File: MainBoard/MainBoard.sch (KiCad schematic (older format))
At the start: 57 parts, among them IC1 MAX30102, J3 Conn_01x30_Female, J6 Conn_01x04, SW1 SW_DIP_x01, SW2 SW_DIP_x01, SW3 SW_DIP_x01, U1 ESP32-WROOM-32, U2 ADP2108AUJ-3.3

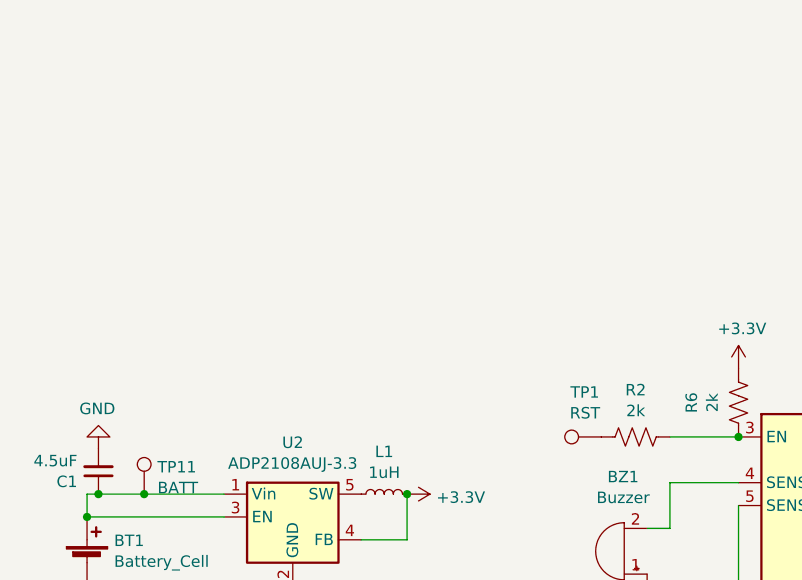
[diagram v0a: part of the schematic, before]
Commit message: add accelerometer and thicken switch traces
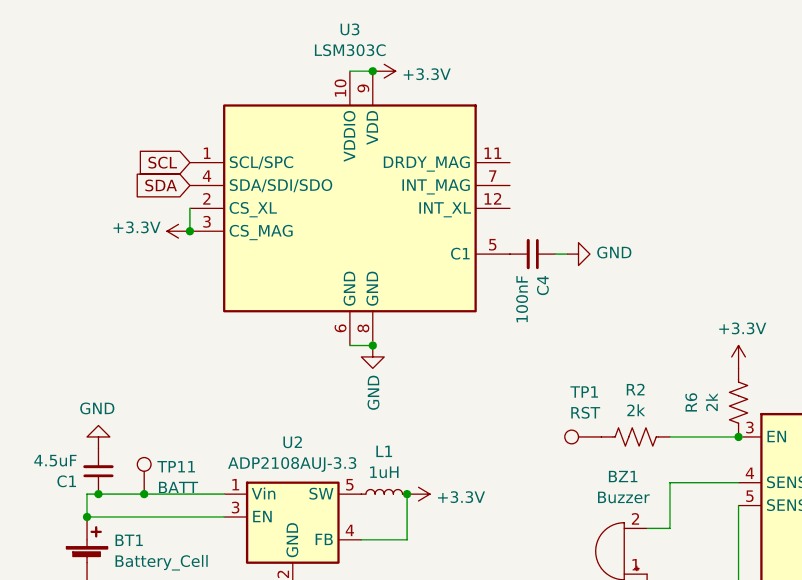
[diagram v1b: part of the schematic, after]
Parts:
- added C4: 100nF, Capacitor_SMD:C_0402_1005Metric, symbol Device:C_Small
- added U3: LSM303C, Package_LGA:LGA-12_2x2mm_P0.5mm, symbol Sensor_Motion:LSM303C
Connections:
- net +3V3: now also U3.10 (VDDIO), U3.2 (CS_XL), U3.3 (CS_MAG), U3.9 (VDD)
- net GND: now also C4.1, U3.6 (GND), U3.8 (GND)
- net SCL: now also U3.1 (SCL/SPC)
- net SDA: now also U3.4 (SDA/SDI/SDO)
- new net: C4.2, U3.5 (C1)
